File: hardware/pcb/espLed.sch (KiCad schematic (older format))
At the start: 3 parts, among them U1 AMS1117-3.3

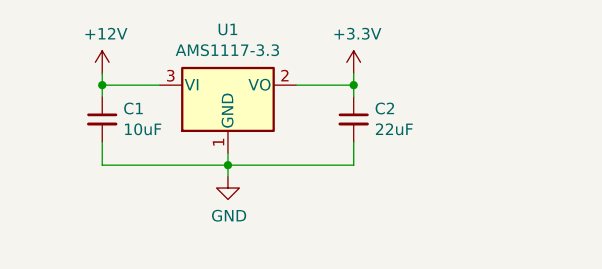
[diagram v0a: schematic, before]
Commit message: add a reverse input voltage protection
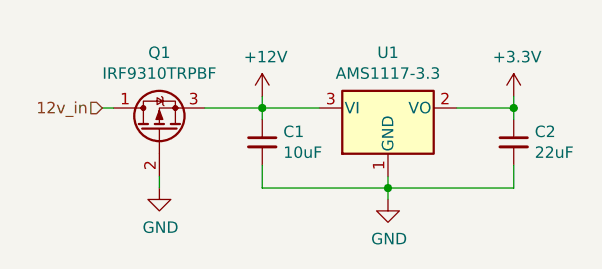
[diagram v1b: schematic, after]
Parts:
- added Q1: IRF9310TRPBF, Package_SO:HSOP-8-1EP_3.9x4.9mm_P1.27mm_EP2.41x3.1mm, symbol Device:Q_PMOS_DGS
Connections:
- net +12V: now also Q1.3 (S)
- net GND: now also Q1.2 (G)
- new net 12v_in: Q1.1 (D)
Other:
- moved on the sheet: C1, C2, U1
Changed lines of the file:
@@
 L Regulator_Linear:AMS1117-3.3 U1
 U 1 1 5FFB1402
-P 1400 950
-F 0 "U1" H 1400 1192 50  0000 C CNN
-F 1 "AMS1117-3.3" H 1400 1101 50  0000 C CNN
-F 2 "Package_TO_SOT_SMD:SOT-223-3_TabPin2" H 1400 1150 50  0001 C CNN
-F 3 "http://www.advanced-monolithic.com/pdf/ds1117.pdf" H 1500 700 50  0001 C CNN
-	1    1400 950
+P 2100 1050
+F 0 "U1" H 2100 1292 50  0000 C CNN
+F 1 "AMS1117-3.3" H 2100 1201 50  0000 C CNN
+F 2 "Package_TO_SOT_SMD:SOT-223-3_TabPin2" H 2100 1250 50  0001 C CNN
+F 3 "http://www.advanced-monolithic.com/pdf/ds1117.pdf" H 2200 800 50  0001 C CNN
+	1    2100 1050
 	1    0    0    -1
 $EndComp
@@
 L Device:C_Small C1
 U 1 1 5FFB8AA8
-P 850 1100
-F 0 "C1" H 942 1146 50  0000 L CNN
-F 1 "10uF" H 942 1055 50  0000 L CNN
-F 2 "" H 850 1100 50  0001 C CNN
-F 3 "~" H 850 1100 50  0001 C CNN
-	1    850  1100
+P 1550 1200
+F 0 "C1" H 1642 1246 50  0000 L CNN
+F 1 "10uF" H 1642 1155 50  0000 L CNN
+F 2 "" H 1550 1200 50  0001 C CNN
+F 3 "~" H 1550 1200 50  0001 C CNN
+	1    1550 1200
 	1    0    0    -1
 $EndComp
@@
 L Device:C_Small C2
 U 1 1 5FFB9EEC
-P 1950 1100
-F 0 "C2" H 2042 1146 50  0000 L CNN
-F 1 "22uF" H 2042 1055 50  0000 L CNN
-F 2 "" H 1950 1100 50  0001 C CNN
-F 3 "~" H 1950 1100 50  0001 C CNN
-	1    1950 1100
+P 2650 1200
+F 0 "C2" H 2742 1246 50  0000 L CNN
+F 1 "22uF" H 2742 1155 50  0000 L CNN
+F 2 "" H 2650 1200 50  0001 C CNN
+F 3 "~" H 2650 1200 50  0001 C CNN
+	1    2650 1200
 	1    0    0    -1
 $EndComp
 Wire Wire Line
-	850  1000 850  950
+	1550 1100 1550 1050
 Wire Wire Line
-	850  950  1100 950
+	1550 1050 1800 1050
 Wire Wire Line
-	1950 950  1950 1000
+	2650 1050 2650 1100
 Wire Wire Line
-	1700 950  1950 950
+	2400 1050 2650 1050
+Connection ~ 1550 1050
 $Comp
-L power:+12V #PWR01
-U 1 1 5FFC54A4
-P 850 900
-F 0 "#PWR01" H 850 750 50  0001 C CNN
-F 1 "+12V" H 865 1073 50  0000 C CNN
-F 2 "" H 850 900 50  0001 C CNN
-F 3 "" H 850 900 50  0001 C CNN
-	1    850  900
+L power:+3.3V #PWR03
+U 1 1 5FFC5BCF
+P 2650 1000
+F 0 "#PWR03" H 2650 850 50  0001 C CNN
+F 1 "+3.3V" H 2665 1173 50  0000 C CNN
+F 2 "" H 2650 1000 50  0001 C CNN
+F 3 "" H 2650 1000 50  0001 C CNN
+	1    2650 1000
 	1    0    0    -1
 $EndComp
 Wire Wire Line
-	850  900  850  950
-Connection ~ 850  950
+	2650 1000 2650 1050
+Connection ~ 2650 1050
+Wire Wire Line
+	1550 1300 1550 1400
+Wire Wire Line
+	1550 1400 2100 1400
+Wire Wire Line
+	2100 1400 2100 1350
+Wire Wire Line
+	2650 1300 2650 1400
+Wire Wire Line
+	2650 1400 2100 1400
+Connection ~ 2100 1400
 $Comp
-L power:+3.3V #PWR03
-U 1 1 5FFC5BCF
-P 1950 900
-F 0 "#PWR03" H 1950 750 50  0001 C CNN
-F 1 "+3.3V" H 1965 1073 50  0000 C CNN
-F 2 "" H 1950 900 50  0001 C CNN
-F 3 "" H 1950 900 50  0001 C CNN
-	1    1950 900
+L power:GND #PWR02
+U 1 1 5FFC65DE
+P 2100 1450
+F 0 "#PWR02" H 2100 1200 50  0001 C CNN
+F 1 "GND" H 2105 1277 50  0000 C CNN
+F 2 "" H 2100 1450 50  0001 C CNN
+F 3 "" H 2100 1450 50  0001 C CNN
+	1    2100 1450
 	1    0    0    -1
 $EndComp
 Wire Wire Line
-	1950 900  1950 950
-Connection ~ 1950 950
-Wire Wire Line
-	850  1200 850  1300
-Wire Wire Line
-	850  1300 1400 1300
-Wire Wire Line
-	1400 1300 1400 1250
-Wire Wire Line
-	1950 1200 1950 1300
-Wire Wire Line
-	1950 1300 1400 1300
-Connection ~ 1400 1300
+	2100 1450 2100 1400
 $Comp
-L power:GND #PWR02
-U 1 1 5FFC65DE
-P 1400 1350
-F 0 "#PWR02" H 1400 1100 50  0001 C CNN
-F 1 "GND" H 1405 1177 50  0000 C CNN
-F 2 "" H 1400 1350 50  0001 C CNN
-F 3 "" H 1400 1350 50  0001 C CNN
-	1    1400 1350
+L Device:Q_PMOS_DGS Q1
+U 1 1 5FFCD3D9
+P 1100 1150
+F 0 "Q1" V 1442 1150 50  0000 C CNN
+F 1 "IRF9310TRPBF" V 1351 1150 50  0000 C CNN
+F 2 "Package_SO:HSOP-8-1EP_3.9x4.9mm_P1.27mm_EP2.41x3.1mm" H 1300 1250 50  0001 C CNN
+F 3 "https://static.chipdip.ru/lib/304/DOC004304962.pdf" H 1100 1150 50  0001 C CNN
+	1    1100 1150
+	0    -1   -1   0
+$EndComp
+$Comp
+L power:GND #PWR04
+U 1 1 5FFD5FC1
+P 1100 1400
+F 0 "#PWR04" H 1100 1150 50  0001 C CNN
+F 1 "GND" H 1105 1227 50  0000 C CNN
+F 2 "" H 1100 1400 50  0001 C CNN
+F 3 "" H 1100 1400 50  0001 C CNN
+	1    1100 1400
 	1    0    0    -1
 $EndComp
 Wire Wire Line
-	1400 1350 1400 1300
+	1100 1400 1100 1350
+Wire Wire Line
+	1550 1050 1300 1050
+$Comp
+L power:+12V #PWR?
+U 1 1 5FFEF1AF
+P 1550 1000
+F 0 "#PWR?" H 1550 850 50  0001 C CNN
+F 1 "+12V" H 1565 1173 50  0000 C CNN
+F 2 "" H 1550 1000 50  0001 C CNN
+F 3 "" H 1550 1000 50  0001 C CNN
+	1    1550 1000
+	1    0    0    -1
+$EndComp
+Wire Wire Line
+	1550 1000 1550 1050
+Text HLabel 850  1050 0    50   Input ~ 0
+12v_in
+Wire Wire Line
+	850  1050 900  1050
 $EndSCHEMATC

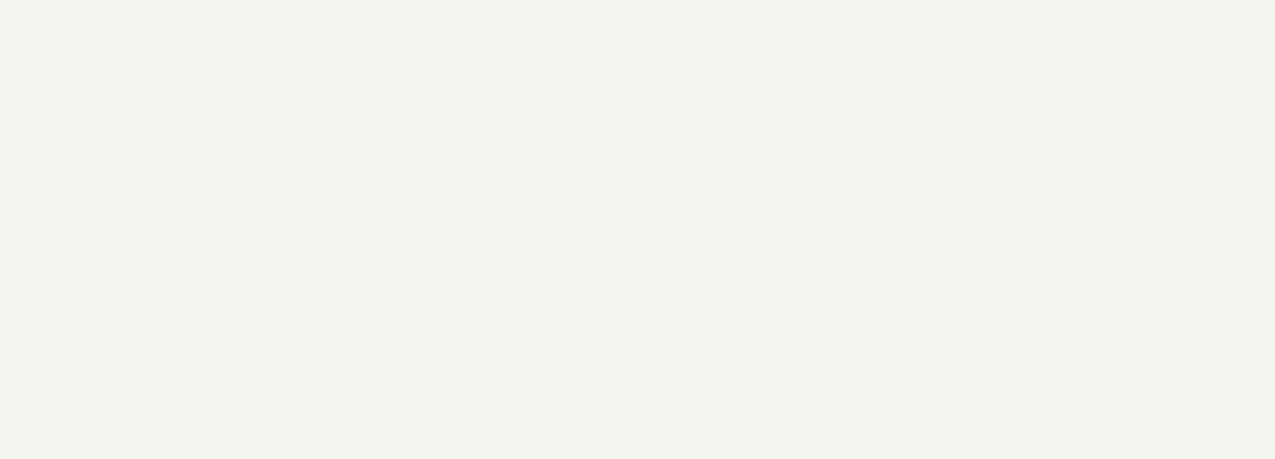
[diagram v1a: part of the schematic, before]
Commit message: layout a basic circuitry for esp-12f
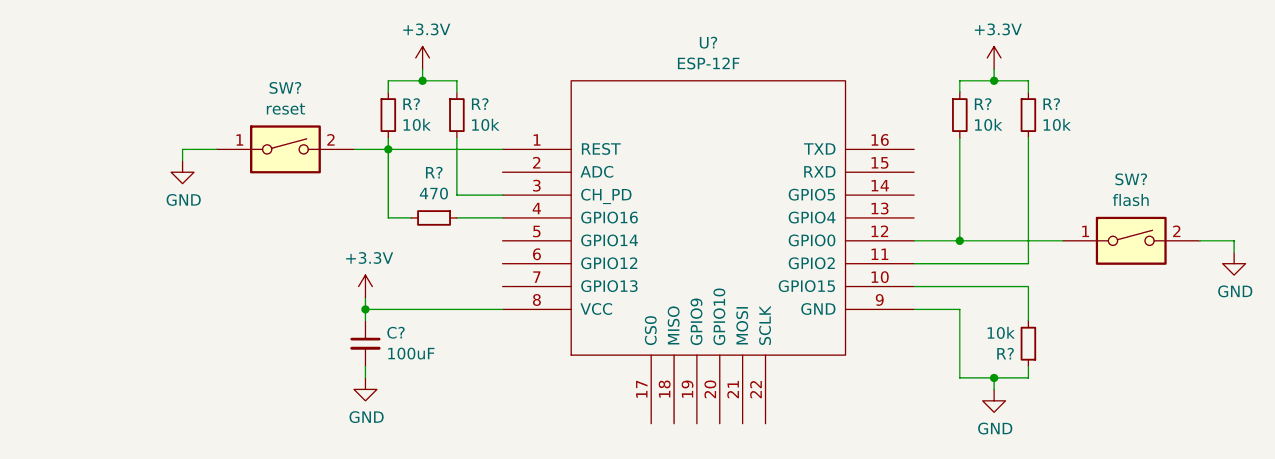
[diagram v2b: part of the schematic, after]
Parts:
- added C?: 100uF, symbol Device:C_Small
- added R? (x5): 10k, symbol Device:R_Small
- added R?: 470, symbol Device:R_Small
- added SW?: reset, symbol Switch:SW_DIP_x01
- added SW?: flash, symbol Switch:SW_DIP_x01
- added U?: ESP-12F, symbol ESP8266:ESP-12F
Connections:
- net +3V3: now also C?.1, R?.1, R?.1, R?.1, R?.1, U?.8 (VCC)
- net GND: now also C?.2, R?.1, SW?.1, SW?.2, U?.9 (GND)
- new net: R?.2, R?.2, SW?.2, U?.1 (REST)
- new net: R?.2, U?.10 (GPIO15)
- new net: R?.2, U?.11 (GPIO2)
- new net: R?.2, SW?.1, U?.12 (GPIO0)
- new net: R?.2, U?.3 (CH_PD)
- new net: R?.1, U?.4 (GPIO16)

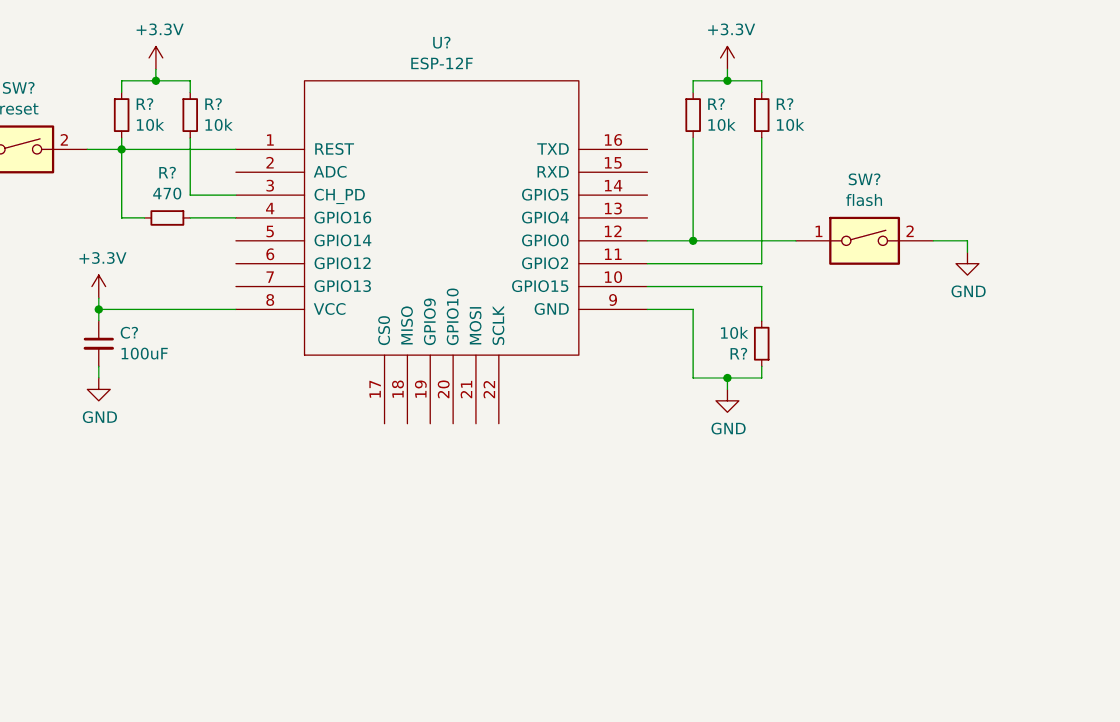
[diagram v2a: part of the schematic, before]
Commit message: add labels for used pins and add connector for flashing
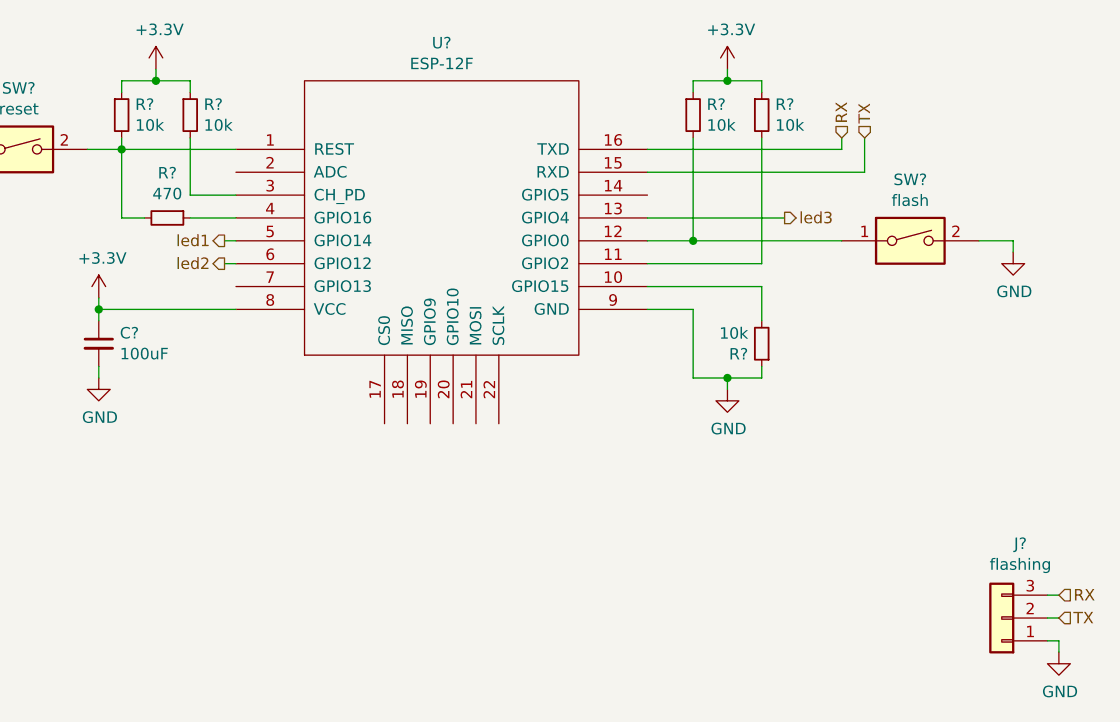
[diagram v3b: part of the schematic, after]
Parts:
- added J?: flashing, symbol Connector_Generic:Conn_01x03
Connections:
- net GND: now also J?.1 (Pin_1)
- net led3: now reaches U?.13 (GPIO4)
- net TX: now reaches U?.15 (RXD)
- net TX: now also J?.2 (Pin_2)
- net RX: now reaches U?.16 (TXD)
- net RX: now also J?.3 (Pin_3)
- net led1: now reaches U?.5 (GPIO14)
- net led2: now reaches U?.6 (GPIO12)
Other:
- moved on the sheet: SW?
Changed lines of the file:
@@
 L Switch:SW_DIP_x01 SW?
 U 1 1 6004F83C
-P 9550 1600
-F 0 "SW?" H 9550 1867 50  0000 C CNN
-F 1 "flash" H 9550 1776 50  0000 C CNN
-F 2 "" H 9550 1600 50  0001 C CNN
-F 3 "~" H 9550 1600 50  0001 C CNN
-	1    9550 1600
+P 9750 1600
+F 0 "SW?" H 9750 1867 50  0000 C CNN
+F 1 "flash" H 9750 1776 50  0000 C CNN
+F 2 "" H 9750 1600 50  0001 C CNN
+F 3 "~" H 9750 1600 50  0001 C CNN
+	1    9750 1600
 	1    0    0    -1
 $EndComp
-Wire Wire Line
-	9250 1600 8800 1600
 Connection ~ 8800 1600
 $Comp
 L power:GND #PWR?
 U 1 1 600519B0
-P 10000 1650
-F 0 "#PWR?" H 10000 1400 50  0001 C CNN
-F 1 "GND" H 10005 1477 50  0000 C CNN
-F 2 "" H 10000 1650 50  0001 C CNN
-F 3 "" H 10000 1650 50  0001 C CNN
-	1    10000 1650
+P 10200 1650
+F 0 "#PWR?" H 10200 1400 50  0001 C CNN
+F 1 "GND" H 10205 1477 50  0000 C CNN
+F 2 "" H 10200 1650 50  0001 C CNN
+F 3 "" H 10200 1650 50  0001 C CNN
+	1    10200 1650
 	1    0    0    -1
 $EndComp
 Wire Wire Line
-	10000 1650 10000 1600
+	10200 1650 10200 1600
 Wire Wire Line
-	10000 1600 9850 1600
+	10200 1600 10050 1600
 $Comp
 L Device:R_Small R?
@@
 Wire Wire Line
 	9100 1800 8600 1800
+Text HLabel 9550 1150 1    50   Input ~ 0
+TX
+Wire Wire Line
+	9550 1150 9550 1300
+Wire Wire Line
+	9550 1300 8600 1300
+Wire Wire Line
+	8600 1200 9450 1200
+Wire Wire Line
+	9450 1200 9450 1150
+Wire Wire Line
+	8800 1600 9450 1600
+Text HLabel 6750 1600 0    50   Output ~ 0
+led1
+Wire Wire Line
+	6750 1600 6800 1600
+Text HLabel 9450 1150 1    50   Input ~ 0
+RX
+Text HLabel 6750 1700 0    50   Output ~ 0
+led2
+Wire Wire Line
+	6800 1700 6750 1700
+Text HLabel 9200 1500 2    50   Output ~ 0
+led3
+Wire Wire Line
+	9200 1500 8600 1500
+Wire Wire Line
+	10400 3350 10350 3350
+Wire Wire Line
+	10400 3400 10400 3350
+$Comp
+L power:GND #PWR?
+U 1 1 6009ECDE
+P 10400 3400
+F 0 "#PWR?" H 10400 3150 50  0001 C CNN
+F 1 "GND" H 10405 3227 50  0000 C CNN
+F 2 "" H 10400 3400 50  0001 C CNN
+F 3 "" H 10400 3400 50  0001 C CNN
+	1    10400 3400
+	1    0    0    -1
+$EndComp
+Wire Wire Line
+	10400 3250 10350 3250
+Text HLabel 10400 3250 2    50   Input ~ 0
+TX
+Wire Wire Line
+	10400 3150 10350 3150
+Text HLabel 10400 3150 2    50   Input ~ 0
+RX
+$Comp
+L Connector_Generic:Conn_01x03 J?
+U 1 1 6009A6C5
+P 10150 3250
+F 0 "J?" H 10068 2925 50  0000 C CNN
+F 1 "flashing" H 10068 3016 50  0000 C CNN
+F 2 "" H 10150 3250 50  0001 C CNN
+F 3 "~" H 10150 3250 50  0001 C CNN
+	1    10150 3250
+	-1   0    0    1
+$EndComp
 $EndSCHEMATC
